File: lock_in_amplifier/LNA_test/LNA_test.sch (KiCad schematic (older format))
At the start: 6 parts, among them J10 A IN, J11 B IN, J12 POWER_IN, J15 I IN, J20 AMP OUT

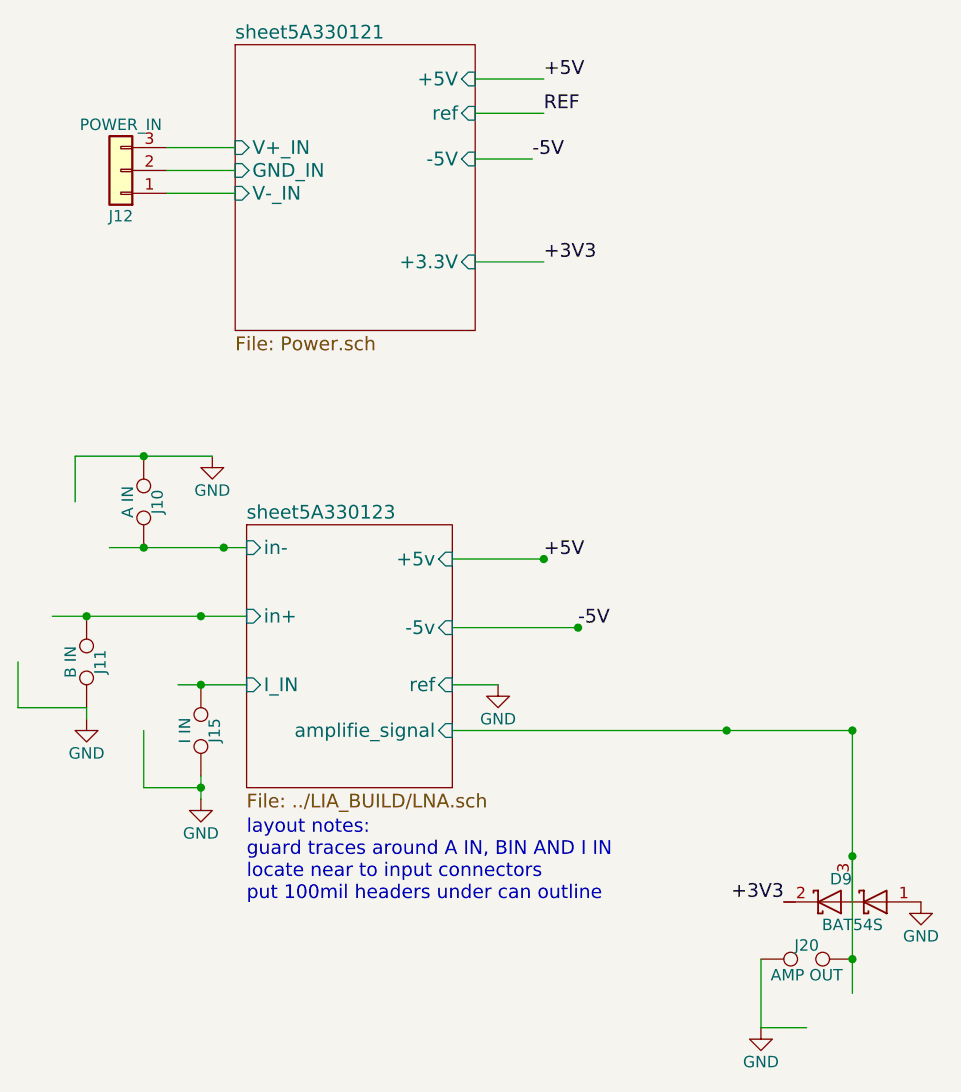
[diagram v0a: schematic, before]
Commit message: initial lna and power floorplan finished.
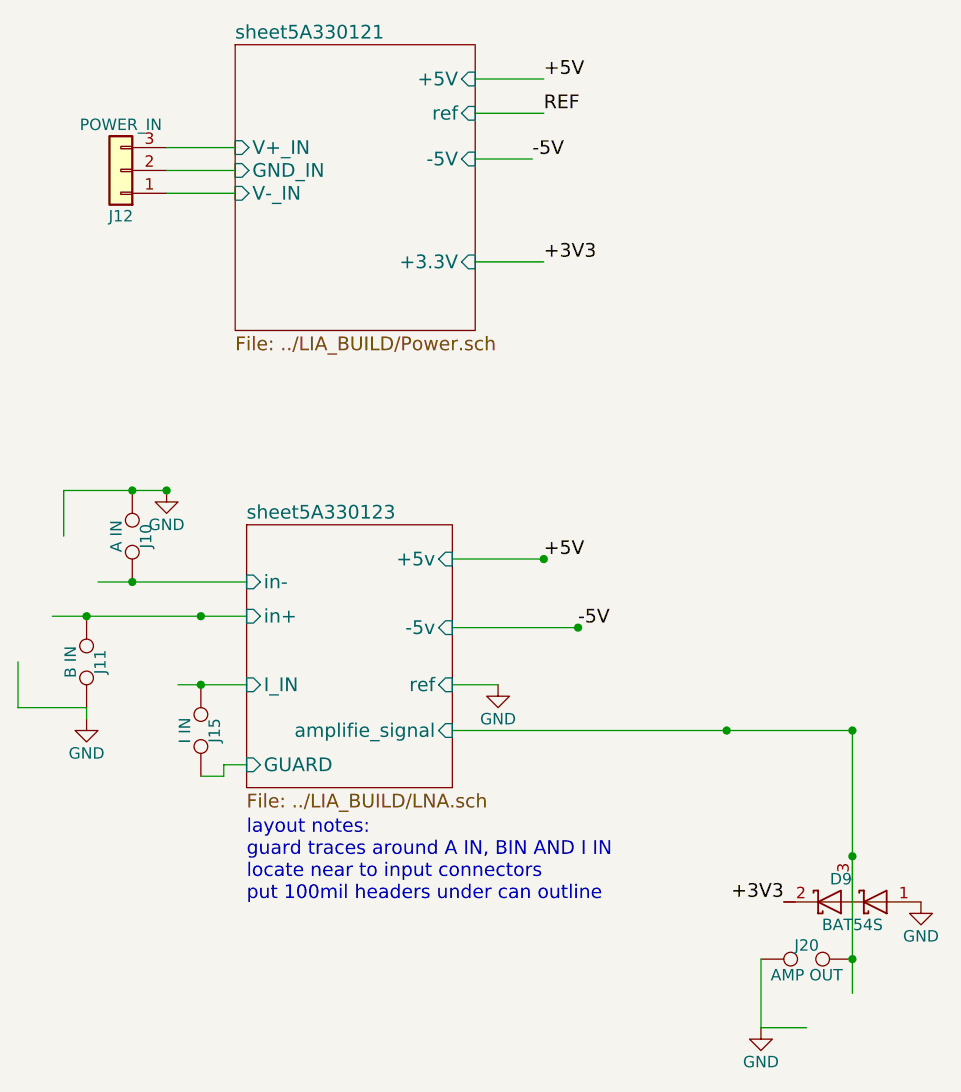
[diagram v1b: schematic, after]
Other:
- moved on the sheet: J10
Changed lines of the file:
@@
 U 5A33012C
 F0 "sheet5A330121" 60
-F1 "Power.sch" 60
+F1 "../LIA_BUILD/Power.sch" 60
 F2 "ref" I R 3400 1250 60
 F3 "+5V" I R 3400 1100 60
@@
 F0 "sheet5A330123" 60
 F1 "../LIA_BUILD/LNA.sch" 60
-F2 "in-" I L 2400 3150 60
+F2 "in-" I L 2400 3300 60
 F3 "in+" I L 2400 3450 60
 F4 "ref" I R 3300 3750 60
@@
 F7 "+5v" I R 3300 3200 60
 F8 "I_IN" I L 2400 3750 60
+F9 "GUARD" I L 2400 4100 60
 $EndSheet
 $Comp
 L TEST_2P J10
 U 1 1 5A330189
-P 1950 2950
-F 0 "J10" H 1950 3010 50  0000 C CNN
-F 1 "A IN" H 1950 2880 50  0000 C CNN
-F 2 "Pin_Headers:Pin_Header_Straight_1x02_Pitch2.54mm" H 1950 2950 50  0001 C CNN
-F 3 "" H 1950 2950 50  0001 C CNN
-	1    1950 2950
+P 1900 3100
+F 0 "J10" H 1900 3160 50  0000 C CNN
+F 1 "A IN" H 1900 3030 50  0000 C CNN
+F 2 "Pin_Headers:Pin_Header_Straight_1x02_Pitch2.54mm" H 1900 3100 50  0001 C CNN
+F 3 "" H 1900 3100 50  0001 C CNN
+	1    1900 3100
 	0    1    1    0
 $EndComp
@@
 $Comp
 L GND #PWR02
-U 1 1 5A33019E
-P 2250 2750
-F 0 "#PWR02" H 2250 2500 50  0001 C CNN
-F 1 "GND" H 2250 2600 50  0000 C CNN
-F 2 "" H 2250 2750 50  0001 C CNN
-F 3 "" H 2250 2750 50  0001 C CNN
-	1    2250 2750
-	1    0    0    -1
-$EndComp
-$Comp
-L GND #PWR03
-U 1 1 5A3301A4
-P 2200 4250
-F 0 "#PWR03" H 2200 4000 50  0001 C CNN
-F 1 "GND" H 2200 4100 50  0000 C CNN
-F 2 "" H 2200 4250 50  0001 C CNN
-F 3 "" H 2200 4250 50  0001 C CNN
-	1    2200 4250
-	1    0    0    -1
-$EndComp
-$Comp
-L GND #PWR04
 U 1 1 5A3301AA
 P 1700 3900
-F 0 "#PWR04" H 1700 3650 50  0001 C CNN
+F 0 "#PWR02" H 1700 3650 50  0001 C CNN
 F 1 "GND" H 1700 3750 50  0000 C CNN
 F 2 "" H 1700 3900 50  0001 C CNN
@@
 $EndComp
 $Comp
-L GND #PWR05
+L GND #PWR03
 U 1 1 5A3301B7
 P 4650 5250
-F 0 "#PWR05" H 4650 5000 50  0001 C CNN
+F 0 "#PWR03" H 4650 5000 50  0001 C CNN
 F 1 "GND" H 4650 5100 50  0000 C CNN
 F 2 "" H 4650 5250 50  0001 C CNN
@@
 	1550 3450 2400 3450
 Wire Wire Line
-	1800 3150 2400 3150
+	1750 3300 2400 3300
 Wire Wire Line
 	2050 1600 2350 1600
@@
 Connection ~ 4500 3950
 Wire Wire Line
-	1650 2750 2250 2750
-Wire Wire Line
-	2200 4150 2200 4250
+	1600 2900 2050 2900
 Connection ~ 2200 3450
 Wire Wire Line
@@
 	4650 5250 4850 5250
 Wire Wire Line
-	1950 3950 1950 4200
-Wire Wire Line
-	1950 4200 2200 4200
-Connection ~ 2200 4200
-Wire Wire Line
-	1650 2950 1650 2750
-Connection ~ 1950 2750
+	1600 3100 1600 2900
+Connection ~ 1900 2900
 Wire Wire Line
 	2100 3750 2400 3750
@@
 	1400 3850 1700 3850
 Connection ~ 1700 3450
-Connection ~ 2300 3150
-Connection ~ 1950 3150
+Connection ~ 1900 3300
 Wire Wire Line
 	3400 1900 3700 1900
@@
 Connection ~ 5050 4500
 $Comp
-L GND #PWR06
+L GND #PWR04
 U 1 1 5A33020E
 P 5350 4700
-F 0 "#PWR06" H 5350 4450 50  0001 C CNN
+F 0 "#PWR04" H 5350 4450 50  0001 C CNN
 F 1 "GND" H 5350 4550 50  0000 C CNN
 F 2 "" H 5350 4700 50  0001 C CNN
@@
 +3V3
 Connection ~ 5050 3950
+Connection ~ 2050 2900
+$Comp
+L GND #PWR05
+U 1 1 5A346E2E
+P 2050 2900
+F 0 "#PWR05" H 2050 2650 50  0001 C CNN
+F 1 "GND" H 2050 2750 50  0000 C CNN
+F 2 "" H 2050 2900 50  0001 C CNN
+F 3 "" H 2050 2900 50  0001 C CNN
+	1    2050 2900
+	1    0    0    -1
+$EndComp
+Wire Wire Line
+	2200 4150 2300 4150
+Wire Wire Line
+	2300 4150 2300 4100
+Wire Wire Line
+	2300 4100 2400 4100
 $EndSCHEMATC
